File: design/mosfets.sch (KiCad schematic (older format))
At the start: 15 parts, among them Q1 IRFS3006, Q2 IRFS3006, Q3 IRFS3006, Q4 IRFS3006, Q5 IRFS3006, Q6 IRFS3006

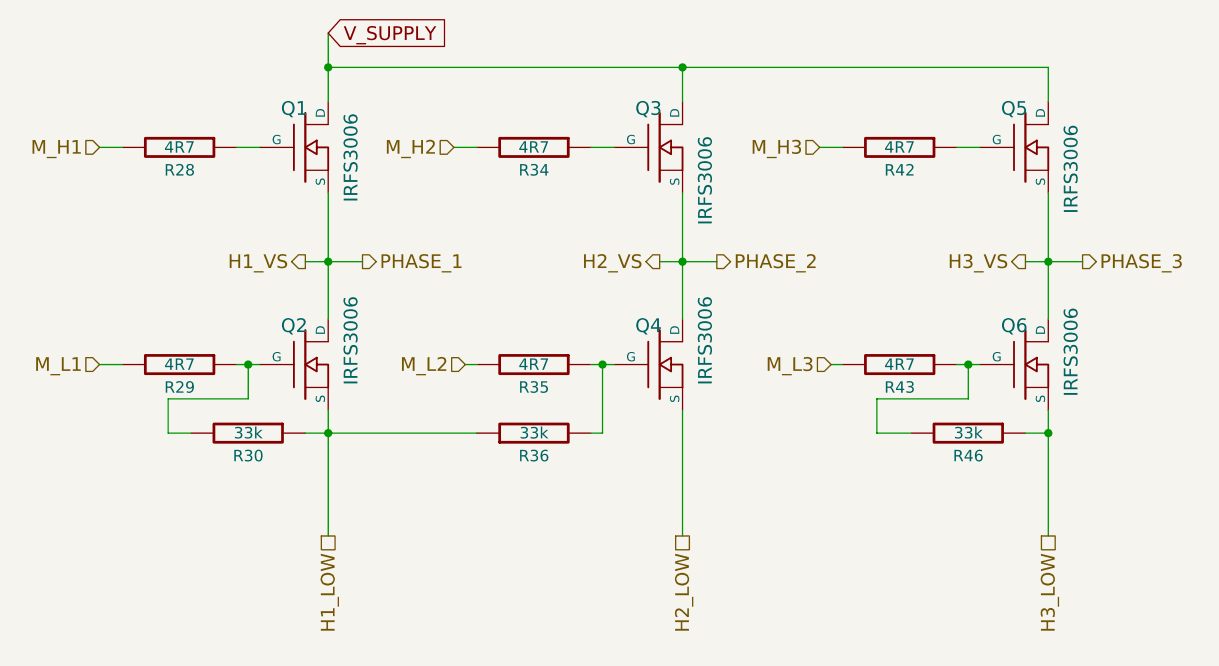
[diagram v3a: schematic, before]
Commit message: Changed voltage divider resistor to 39k
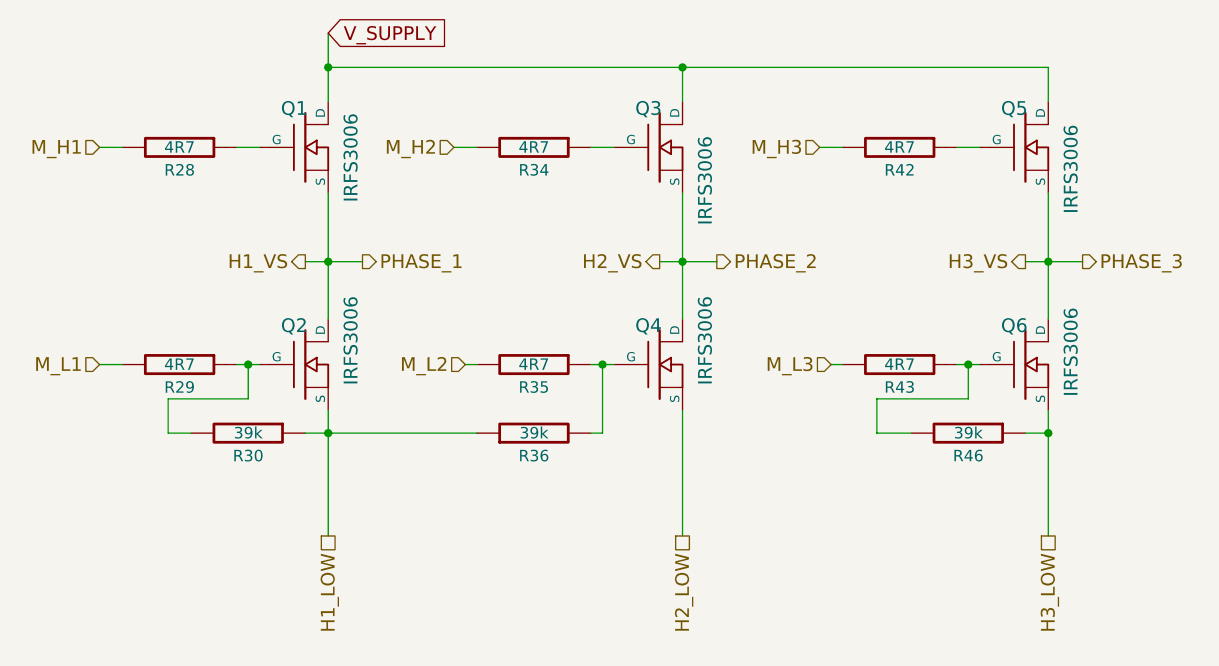
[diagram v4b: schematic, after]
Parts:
- R30, R36, R46: value 33k -> 39k
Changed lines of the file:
@@
 LIBS:crf_1
 LIBS:BLDC_4-cache
-EELAYER 25 0
+EELAYER 24 0
 EELAYER END
 $Descr A4 11693 8268
@@
 P 7850 4050
 F 0 "R46" V 7950 4050 50  0000 C CNN
-F 1 "33k" V 7850 4050 50  0000 C CNN
+F 1 "39k" V 7850 4050 50  0000 C CNN
 F 2 "SMD_Packages:SMD-0603_r" H 7850 4050 60  0001 C CNN
 F 3 "" H 7850 4050 60  0001 C CNN
@@
 P 4700 4050
 F 0 "R30" V 4800 4050 50  0000 C CNN
-F 1 "33k" V 4700 4050 50  0000 C CNN
+F 1 "39k" V 4700 4050 50  0000 C CNN
 F 2 "SMD_Packages:SMD-0603_r" H 4700 4050 60  0001 C CNN
 F 3 "" H 4700 4050 60  0001 C CNN
@@
 P 5950 4050
 F 0 "R36" V 5850 4050 50  0000 C CNN
-F 1 "33k" V 5950 4050 50  0000 C CNN
+F 1 "39k" V 5950 4050 50  0000 C CNN
 F 2 "SMD_Packages:SMD-0603_r" H 5950 4050 60  0001 C CNN
 F 3 "" H 5950 4050 60  0001 C CNN
@@
 F8 14 F0 0B 42 92 4F 42 07 35 54 00 00 00 00 00 00 7A 11 BC 6D 0C 00 00 00 00 00 F4 2D 50 43 05
 00 00 00 00 00 7D 0B D4 50 01 00 00 00 00 40 DF 02 35 54 00 00 00 00 00 D0 B7 FC 1F 55 28 1C 02
-4B 67 87 83 00 00 00 00 49 45 4E 44 AE 42 60 82 F0
+4B 67 87 83 00 00 00 00 49 45 4E 44 AE 42 60 82 8B
 EndData
 $EndBitmap
@@
 6D 12 06 83 C1 60 DA 0B D8 26 61 30 18 0C A6 BD 80 6D 12 06 83 C1 60 DA 0B D8 26 61 30 18 0C A6
 BD 80 6D 12 06 83 C1 60 DA 0B FF 03 68 C2 AC 3A A9 DC 0C E9 00 00 00 00 49 45 4E 44 AE 42 60 82
-B8
+63
 EndData
 $EndBitmap
@@
 50 A9 E8 5E 5D 3A 9D 4E 20 10 38 47 FD BC E9 C5 23 08 52 5C 54 54 5F 5F 3F 46 5C 9C 4C 26 63 A3
 F8 9F 0A E6 43 31 30 BE 81 FA D0 5F 5D 10 8C 7F 13 D8 9A 12 06 06 06 06 EF 60 3E 14 03 03 03 83
-77 FE 07 75 CC 31 C3 52 8F 7C 35 00 00 00 00 49 45 4E 44 AE 42 60 82 00
+77 FE 07 75 CC 31 C3 52 8F 7C 35 00 00 00 00 49 45 4E 44 AE 42 60 82 BB
 EndData
 $EndBitmap
@@
 40 20 9C 12 44 46 09 04 02 E1 94 20 EE F7 67 02 30 C1 25 10 08 E7 25 24 1A 25 10 08 84 53 82 2C
 11 21 10 08 84 53 82 44 A3 04 02 81 70 4A 10 19 25 10 08 84 53 82 C8 28 81 40 20 9C 12 FF 1F 3E
-01 30 64 8D 18 65 07 00 00 00 00 49 45 4E 44 AE 42 60 82 CB
+01 30 64 8D 18 65 07 00 00 00 00 49 45 4E 44 AE 42 60 82 83
 EndData
 $EndBitmap

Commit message: Changed FETs and VREG part number to make things a bit more clear
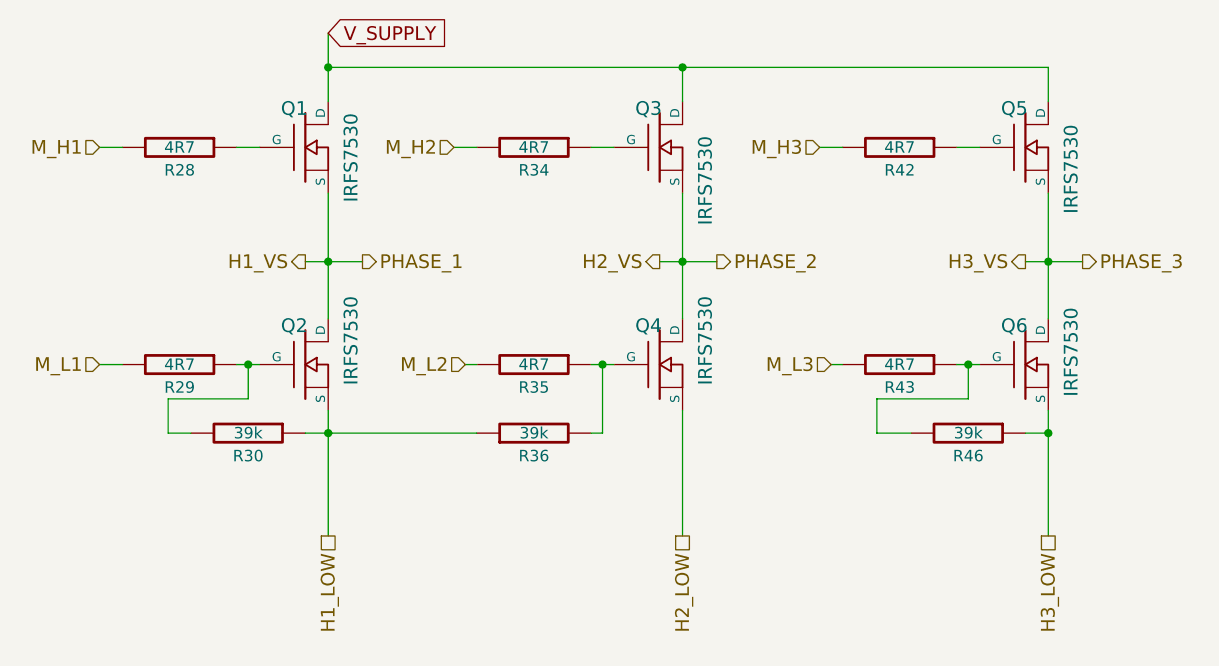
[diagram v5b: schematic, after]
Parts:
- Q1, Q2, Q3, Q4, Q5, Q6: value IRFS3006 -> IRFS7530

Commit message: HW4.8: better shunt routing, extra pin on comm connector, footprint fixed, zone fixes, many other improvements
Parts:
- R28, R29, R30, R34, R35, R36, R42, R43, R46: footprint SMD_Packages:SMD-0603_r -> CRF1:SMD-0603_r; symbol R -> R-RESCUE-BLDC_4
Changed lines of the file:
@@
 EESchema Schematic File Version 2
+LIBS:BLDC_4-rescue
 LIBS:power
 LIBS:device
@@
 LIBS:crf_1
 LIBS:BLDC_4-cache
-EELAYER 24 0
+EELAYER 25 0
 EELAYER END
 $Descr A4 11693 8268
 encoding utf-8
 Sheet 2 7
-Title "BLDC Driver 4.6"
-Date "25 Aug 2014"
-Rev "4.6"
+Title "BLDC Driver 4.8"
+Date "21 aug 2015"
+Rev "4.8"
 Comp "Benjamin Vedder"
 Comment1 ""
@@
 $EndDescr
 $Comp
-L R R46
+L R-RESCUE-BLDC_4 R46
 U 1 1 53F8E60B
 P 7850 4050
 F 0 "R46" V 7950 4050 50  0000 C CNN
 F 1 "39k" V 7850 4050 50  0000 C CNN
-F 2 "SMD_Packages:SMD-0603_r" H 7850 4050 60  0001 C CNN
+F 2 "CRF1:SMD-0603_r" H 7850 4050 60  0001 C CNN
 F 3 "" H 7850 4050 60  0001 C CNN
 	1    7850 4050
@@
 $EndComp
 $Comp
-L R R30
+L R-RESCUE-BLDC_4 R30
 U 1 1 53F8E612
 P 4700 4050
 F 0 "R30" V 4800 4050 50  0000 C CNN
 F 1 "39k" V 4700 4050 50  0000 C CNN
-F 2 "SMD_Packages:SMD-0603_r" H 4700 4050 60  0001 C CNN
+F 2 "CRF1:SMD-0603_r" H 4700 4050 60  0001 C CNN
 F 3 "" H 4700 4050 60  0001 C CNN
 	1    4700 4050
@@
 $EndComp
 $Comp
-L R R29
+L R-RESCUE-BLDC_4 R29
 U 1 1 53F8E64B
 P 4400 3750
 F 0 "R29" V 4500 3750 50  0000 C CNN
 F 1 "4R7" V 4400 3750 50  0000 C CNN
-F 2 "SMD_Packages:SMD-0603_r" H 4400 3750 60  0001 C CNN
+F 2 "CRF1:SMD-0603_r" H 4400 3750 60  0001 C CNN
 F 3 "" H 4400 3750 60  0001 C CNN
 	1    4400 3750
@@
 $EndComp
 $Comp
-L R R28
+L R-RESCUE-BLDC_4 R28
 U 1 1 53F8E652
 P 4400 2800
 F 0 "R28" V 4500 2800 50  0000 C CNN
 F 1 "4R7" V 4400 2800 50  0000 C CNN
-F 2 "SMD_Packages:SMD-0603_r" H 4400 2800 60  0001 C CNN
+F 2 "CRF1:SMD-0603_r" H 4400 2800 60  0001 C CNN
 F 3 "" H 4400 2800 60  0001 C CNN
 	1    4400 2800
@@
 $EndComp
 $Comp
-L R R34
+L R-RESCUE-BLDC_4 R34
 U 1 1 53F8E65E
 P 5950 2800
 F 0 "R34" V 6050 2800 50  0000 C CNN
 F 1 "4R7" V 5950 2800 50  0000 C CNN
-F 2 "SMD_Packages:SMD-0603_r" H 5950 2800 60  0001 C CNN
+F 2 "CRF1:SMD-0603_r" H 5950 2800 60  0001 C CNN
 F 3 "" H 5950 2800 60  0001 C CNN
 	1    5950 2800
@@
 $EndComp
 $Comp
-L R R35
+L R-RESCUE-BLDC_4 R35
 U 1 1 53F8E665
 P 5950 3750
 F 0 "R35" V 6050 3750 50  0000 C CNN
 F 1 "4R7" V 5950 3750 50  0000 C CNN
-F 2 "SMD_Packages:SMD-0603_r" H 5950 3750 60  0001 C CNN
+F 2 "CRF1:SMD-0603_r" H 5950 3750 60  0001 C CNN
 F 3 "" H 5950 3750 60  0001 C CNN
 	1    5950 3750
@@
 $EndComp
 $Comp
-L R R43
+L R-RESCUE-BLDC_4 R43
 U 1 1 53F8E688
 P 7550 3750
 F 0 "R43" V 7650 3750 50  0000 C CNN
 F 1 "4R7" V 7550 3750 50  0000 C CNN
-F 2 "SMD_Packages:SMD-0603_r" H 7550 3750 60  0001 C CNN
+F 2 "CRF1:SMD-0603_r" H 7550 3750 60  0001 C CNN
 F 3 "" H 7550 3750 60  0001 C CNN
 	1    7550 3750
@@
 $EndComp
 $Comp
-L R R42
+L R-RESCUE-BLDC_4 R42
 U 1 1 53F8E68F
 P 7550 2800
 F 0 "R42" V 7650 2800 50  0000 C CNN
 F 1 "4R7" V 7550 2800 50  0000 C CNN
-F 2 "SMD_Packages:SMD-0603_r" H 7550 2800 60  0001 C CNN
+F 2 "CRF1:SMD-0603_r" H 7550 2800 60  0001 C CNN
 F 3 "" H 7550 2800 60  0001 C CNN
 	1    7550 2800
@@
 $EndComp
 $Comp
-L R R36
+L R-RESCUE-BLDC_4 R36
 U 1 1 53F8E69C
 P 5950 4050
 F 0 "R36" V 5850 4050 50  0000 C CNN
 F 1 "39k" V 5950 4050 50  0000 C CNN
-F 2 "SMD_Packages:SMD-0603_r" H 5950 4050 60  0001 C CNN
+F 2 "CRF1:SMD-0603_r" H 5950 4050 60  0001 C CNN
 F 3 "" H 5950 4050 60  0001 C CNN
 	1    5950 4050
@@
 00 00 00 41 83 58 05 00 00 08 1A C4 2A 00 00 40 D0 20 56 01 00 00 82 06 B1 0A 00 00 10 34 88 55
 00 00 80 A0 41 AC 02 00 00 04 CD FF 03 15 B2 0E 9E 1D 9F E2 F2 00 00 00 00 49 45 4E 44 AE 42 60
-82 FA
+82 97
 EndData
 $EndBitmap
